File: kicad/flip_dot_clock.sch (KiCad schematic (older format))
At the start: 11 parts, among them U0 TPS62177DQC, U2 NCV7719

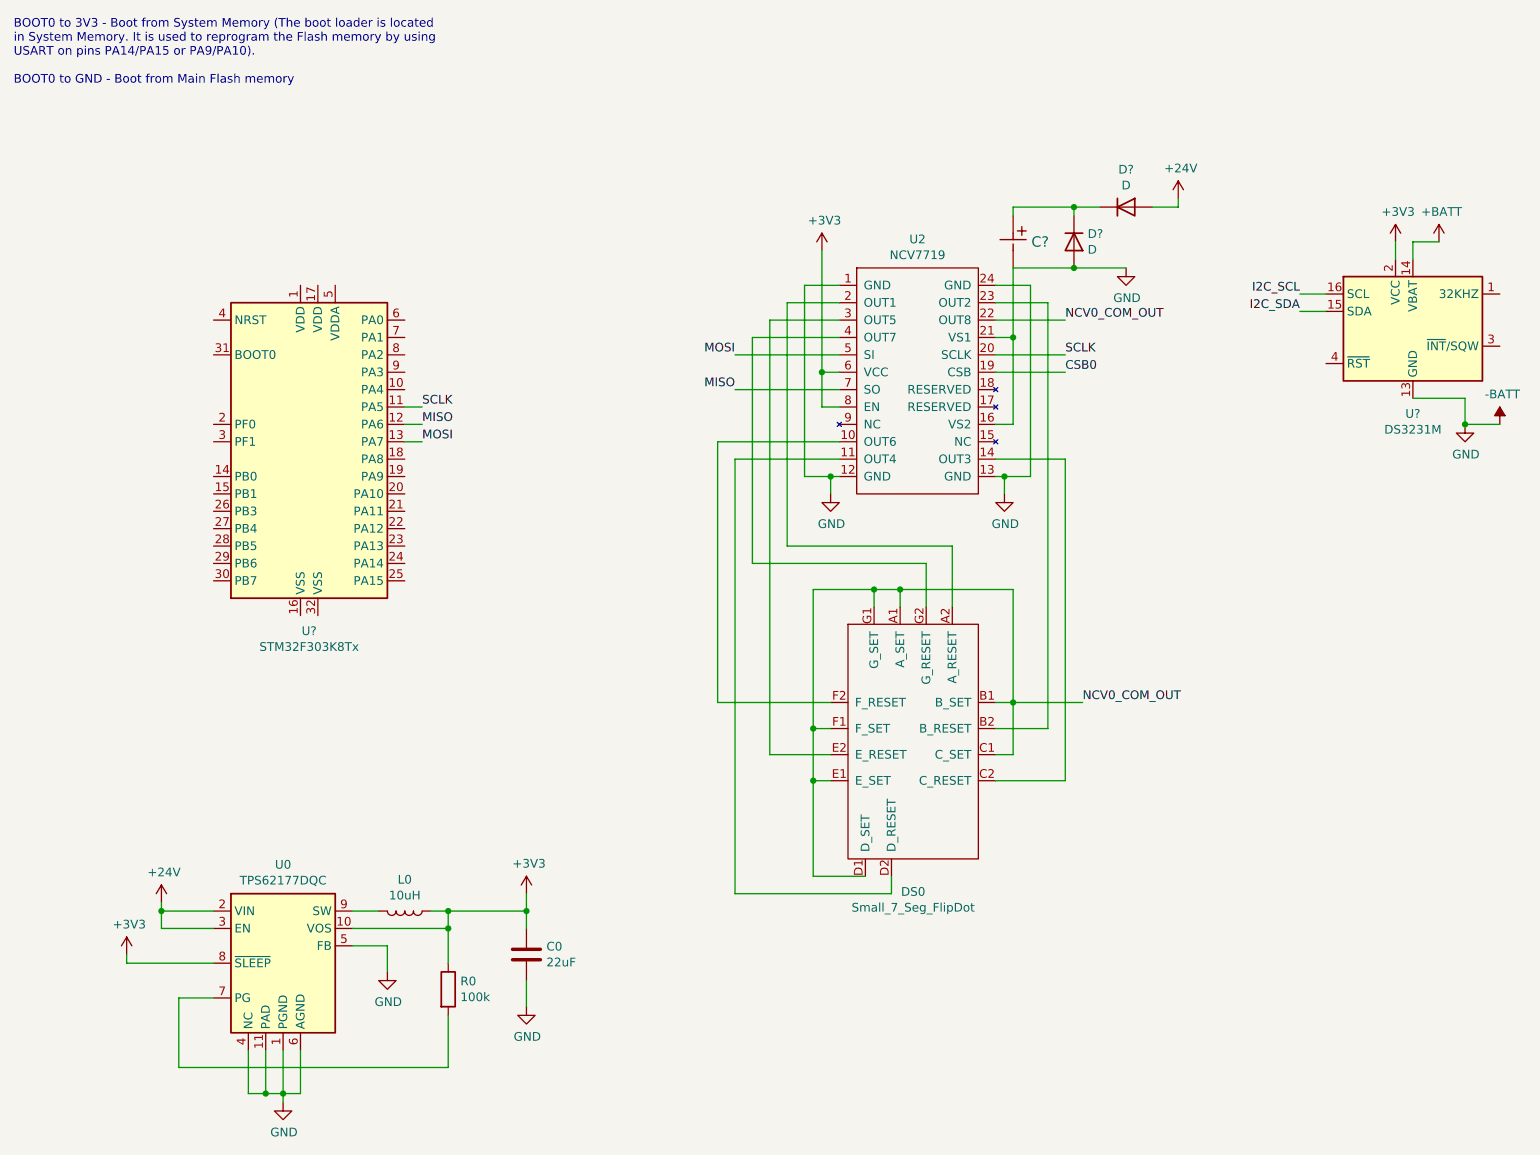
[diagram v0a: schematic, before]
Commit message: seven segment holder pcb
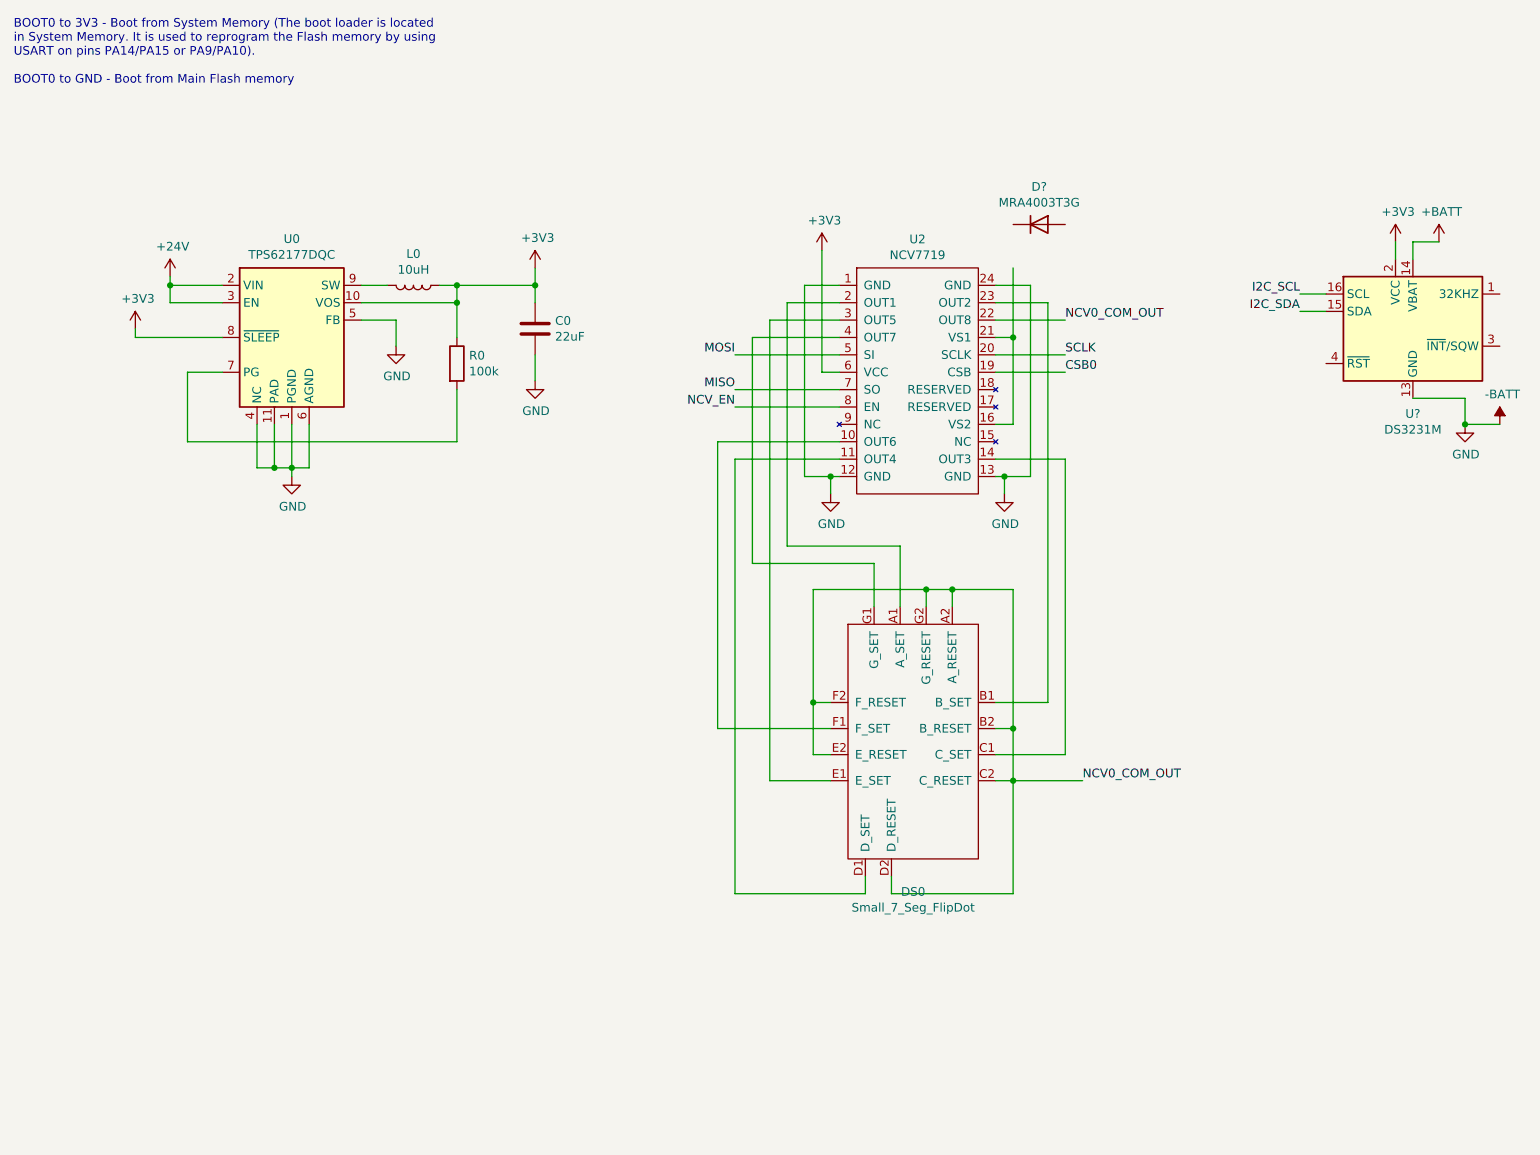
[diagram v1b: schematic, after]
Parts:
- removed C?: UCD1V101MNL1GS, PCAP_8x10-ELECT, symbol mio:UCD1V101MNL1GS
- removed D? (x2): D, symbol Device:D
- removed U?: STM32F303K8Tx, Package_QFP:LQFP-32_7x7mm_P0.8mm, symbol MCU_ST_STM32F3:STM32F303K8Tx
- added D?: MRA4003T3G, Diode_SMD:D_SMA, symbol Diode:MRA4003T3G
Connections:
- net +3V3: no longer U2.8 (EN)
- net -BATT: no longer U2.16 (VS2), U2.21 (VS1)
- net NCV0_COM_OUT: now also DS0.A2 (A_RESET), DS0.B2 (B_RESET), DS0.C2 (C_RESET), DS0.D2 (D_RESET), DS0.E2 (E_RESET), DS0.F2 (F_RESET), DS0.G2 (G_RESET); no longer DS0.A1 (A_SET), DS0.B1 (B_SET), DS0.C1 (C_SET), DS0.D1 (D_SET), DS0.E1 (E_SET), DS0.F1 (F_SET), DS0.G1 (G_SET)
- net at U2.10 (OUT6): now also DS0.F1 (F_SET); no longer DS0.F2 (F_RESET)
- net at U2.11 (OUT4): now also DS0.D1 (D_SET); no longer DS0.D2 (D_RESET)
- net at U2.14 (OUT3): now also DS0.C1 (C_SET); no longer DS0.C2 (C_RESET)
- net at U2.2 (OUT1): now also DS0.A1 (A_SET); no longer DS0.A2 (A_RESET)
- net at U2.23 (OUT2): now also DS0.B1 (B_SET); no longer DS0.B2 (B_RESET)
- net at U2.3 (OUT5): now also DS0.E1 (E_SET); no longer DS0.E2 (E_RESET)
- net at U2.4 (OUT7): now also DS0.G1 (G_SET); no longer DS0.G2 (G_RESET)
- new net: U2.16 (VS2), U2.21 (VS1)
- new net NCV_EN: U2.8 (EN)
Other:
- moved on the sheet: C0, L0, R0, U0
